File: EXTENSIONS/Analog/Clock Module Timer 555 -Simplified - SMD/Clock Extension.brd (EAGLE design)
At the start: 20 x 48 mm, 8 parts, among them X1 USB-A

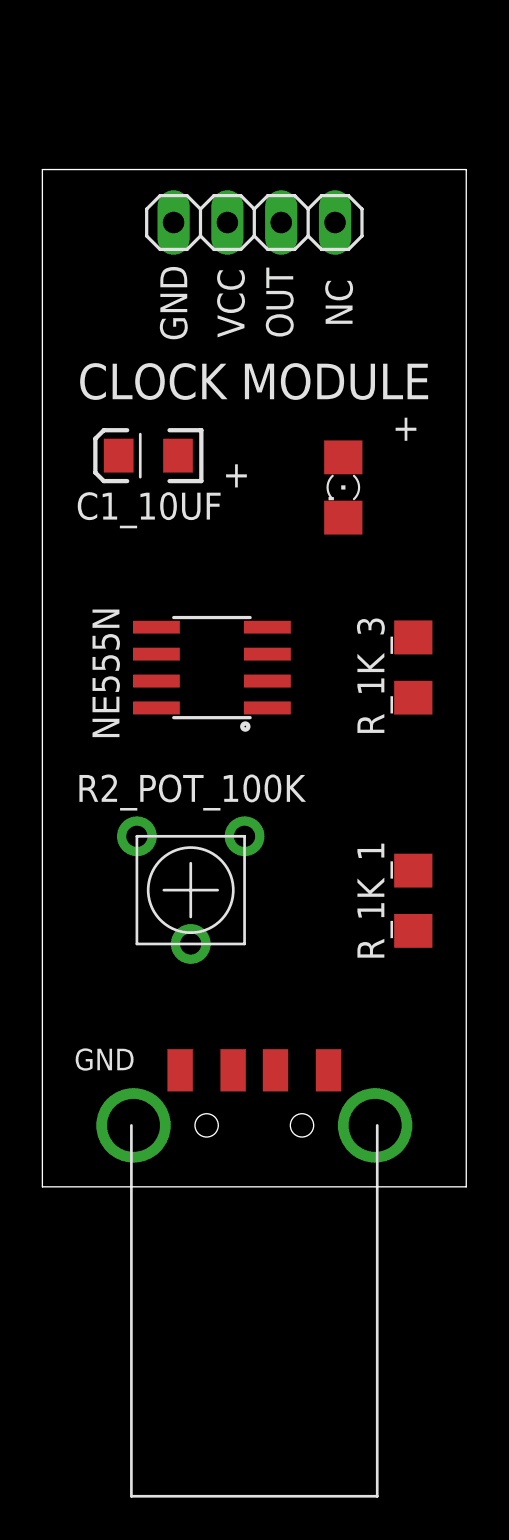
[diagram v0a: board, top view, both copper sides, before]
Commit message: Create new clock module SMD
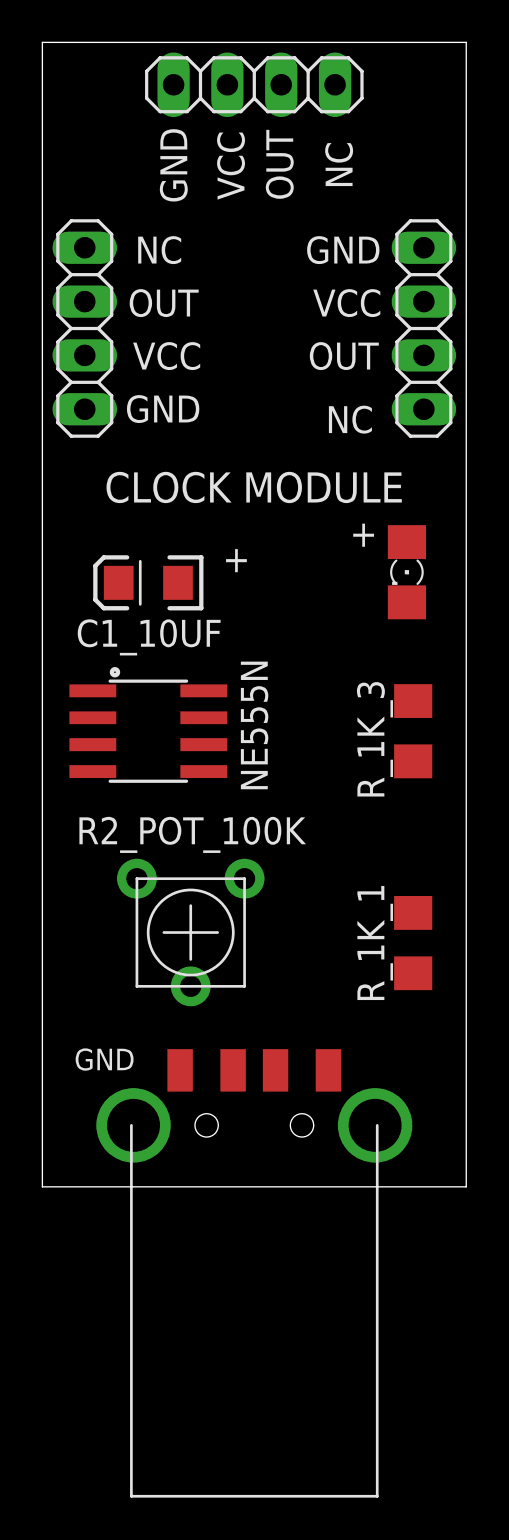
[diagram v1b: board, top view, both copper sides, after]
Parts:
- removed JP1: (no value), pinhead:1X04
- added OUT_1, OUT_2, OUT_3: (no value), pinhead:1X04
- moved C1_10UF 6.00 mm to (7.00, 40.5)
- moved LED_OUTPUT 5.00 mm to (19.2, 41.0)
- moved NE555N 4.24 mm to (7.00, 33.5), turned to 270 degrees
- moved R_1K_3 3.00 mm to (19.5, 33.5)
- moved R2_POT_100K 2.00 mm to (9.00, 24.0)
- moved R_1K_1 2.00 mm to (19.5, 23.5)
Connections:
- removed net TMR555_OUTPUT_REVERSE: JP1.4
- net GND: now also OUT_1.1, OUT_2.1, OUT_3.1; no longer JP1.1
- net TMR555_OUTPUT: now also OUT_1.3, OUT_2.3, OUT_3.3; no longer JP1.3
- net VCC: now also OUT_1.2, OUT_2.2, OUT_3.2; no longer JP1.2
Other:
- board size 20 x 48 mm -> 20 x 54 mm
- board text added: "PCBv1/SMD - 2019.12"
- board text removed: "PCBv3 - 2019.08"

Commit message: Fix bug in 4017-7Segment v2
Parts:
- moved LED_OUTPUT 13.0 mm to (12.2, 52.0)
- moved C1_10UF 5.10 mm to (12.0, 41.5)
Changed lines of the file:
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@@
 <text x="12" y="45" size="1.4224" layer="25" align="center">CLOCK MODULE</text>
 <text x="10.5" y="41" size="1.27" layer="25">+</text>
-<text x="16.5" y="42.2" size="1.27" layer="25">+</text>
+<text x="11.5" y="55.2" size="1.27" layer="25">+</text>
 <text x="16.2" y="56.2" size="1.27" layer="25" rot="R180" align="center">GND</text>
 <text x="16.4" y="53.7" size="1.27" layer="25" rot="R180" align="center">VCC</text>
@@
 <attribute name="VALUE" x="5.825" y="24" size="0.6096" layer="27" rot="R180"/>
 </element>
-<element name="LED_OUTPUT" library="adafruit" package="1206" value="" x="19.2" y="41" smashed="yes" rot="R270">
-<attribute name="VALUE" x="16.66" y="42.27" size="1.27" layer="27" rot="R270"/>
+<element name="LED_OUTPUT" library="adafruit" package="1206" value="" x="12.2" y="52" smashed="yes" rot="R270">
+<attribute name="VALUE" x="9.66" y="53.27" size="1.27" layer="27" rot="R270"/>
 </element>
 <element name="R_1K_3" library="adafruit" package="R1206" value="" x="19.5" y="33.5" smashed="yes" rot="R90">
@@
 <attribute name="VALUE" x="21.913" y="32.103" size="1.27" layer="27" rot="R90"/>
 </element>
-<element name="C1_10UF" library="SparkFun-Capacitors" package="EIA3216" value="10uF" x="7" y="40.5" smashed="yes" rot="R180">
-<attribute name="PROD_ID" value="CAP-00811" x="7" y="40.5" size="1.778" layer="27" rot="R180" display="off"/>
-<attribute name="NAME" x="7.04" y="38.119" size="1.27" layer="25" rot="R180" align="center"/>
-<attribute name="VALUE" x="6.592" y="39.168" size="0.4064" layer="27" rot="R180"/>
+<element name="C1_10UF" library="SparkFun-Capacitors" package="EIA3216" value="10uF" x="12" y="41.5" smashed="yes" rot="R180">
+<attribute name="PROD_ID" value="CAP-00811" x="12" y="41.5" size="1.778" layer="27" rot="R180" display="off"/>
+<attribute name="NAME" x="12.04" y="39.119" size="1.27" layer="25" rot="R180" align="center"/>
+<attribute name="VALUE" x="11.592" y="40.168" size="0.4064" layer="27" rot="R180"/>
 </element>
 <element name="NE555N" library="SparkFun-AnalogIC" package="SO08" value="" x="7" y="33.5" smashed="yes" rot="R270">
@@
 <contactref element="OUT_3" pad="1"/>
 <wire x1="8.19" y1="64" x2="20" y2="56.31" width="0" layer="19" extent="1-1"/>
-<wire x1="5.6" y1="40.5" x2="20" y2="56.31" width="0" layer="19" extent="1-1"/>
-<wire x1="4.3838" y1="35.405" x2="5.6" y2="40.5" width="0" layer="19" extent="1-1"/>
-<wire x1="19.5" y1="32.078" x2="4.3838" y2="35.405" width="0" layer="19" extent="1-1"/>
+<wire x1="4" y1="48.69" x2="8.19" y2="64" width="0" layer="19" extent="1-1"/>
+<wire x1="10.6" y1="41.5" x2="4" y2="48.69" width="0" layer="19" extent="1-1"/>
+<wire x1="4.3838" y1="35.405" x2="10.6" y2="41.5" width="0" layer="19" extent="1-1"/>
+<wire x1="19.5" y1="32.078" x2="10.6" y2="41.5" width="0" layer="19" extent="1-1"/>
 <wire x1="8.5" y1="17.5" x2="19.5" y2="32.078" width="0" layer="19" extent="1-1"/>
-<wire x1="4" y1="48.69" x2="8.5" y2="17.5" width="0" layer="19" extent="1-1"/>
 </signal>
 <signal name="VCC">
@@
 <contactref element="OUT_3" pad="2"/>
 <wire x1="20" y1="53.77" x2="10.73" y2="64" width="0" layer="19" extent="1-1"/>
-<wire x1="9.6162" y1="35.405" x2="20" y2="53.77" width="0" layer="19" extent="1-1"/>
+<wire x1="4" y1="51.23" x2="10.73" y2="64" width="0" layer="19" extent="1-1"/>
+<wire x1="9.6162" y1="35.405" x2="4" y2="51.23" width="0" layer="19" extent="1-1"/>
 <wire x1="4.3838" y1="31.595" x2="9.6162" y2="35.405" width="0" layer="19" extent="1-1"/>
 <wire x1="19.5" y1="24.922" x2="9.6162" y2="35.405" width="0" layer="19" extent="1-1"/>
 <wire x1="15.5" y1="17.5" x2="19.5" y2="24.922" width="0" layer="19" extent="1-1"/>
-<wire x1="4" y1="51.23" x2="15.5" y2="17.5" width="0" layer="19" extent="1-1"/>
 </signal>
 <signal name="DIS">
@@
 <contactref element="NE555N" pad="2"/>
 <contactref element="NE555N" pad="6"/>
-<wire x1="4.3838" y1="34.135" x2="8.4" y2="40.5" width="0" layer="19" extent="1-1"/>
-<wire x1="9.6162" y1="32.865" x2="4.3838" y2="34.135" width="0" layer="19" extent="1-1"/>
+<wire x1="9.6162" y1="32.865" x2="13.4" y2="41.5" width="0" layer="19" extent="1-1"/>
+<wire x1="4.3838" y1="34.135" x2="9.6162" y2="32.865" width="0" layer="19" extent="1-1"/>
 <wire x1="9" y1="21.46" x2="9.6162" y2="32.865" width="0" layer="19" extent="1-1"/>
 </signal>
@@
 <contactref element="OUT_2" pad="3"/>
 <contactref element="OUT_3" pad="3"/>
-<wire x1="20" y1="51.23" x2="13.27" y2="64" width="0" layer="19" extent="1-1"/>
-<wire x1="19.2" y1="42.422" x2="20" y2="51.23" width="0" layer="19" extent="1-1"/>
-<wire x1="4.3838" y1="32.865" x2="19.2" y2="42.422" width="0" layer="19" extent="1-1"/>
-<wire x1="4" y1="53.77" x2="4.3838" y2="32.865" width="0" layer="19" extent="1-1"/>
+<wire x1="12.2" y1="53.422" x2="13.27" y2="64" width="0" layer="19" extent="1-1"/>
+<wire x1="20" y1="51.23" x2="12.2" y2="53.422" width="0" layer="19" extent="1-1"/>
+<wire x1="4" y1="53.77" x2="12.2" y2="53.422" width="0" layer="19" extent="1-1"/>
+<wire x1="4.3838" y1="32.865" x2="4" y2="53.77" width="0" layer="19" extent="1-1"/>
 </signal>
 <signal name="N$5">
 <contactref element="LED_OUTPUT" pad="C"/>
 <contactref element="R_1K_3" pad="2"/>
-<wire x1="19.5" y1="34.922" x2="19.2" y2="39.578" width="0" layer="19" extent="1-1"/>
+<wire x1="19.5" y1="34.922" x2="12.2" y2="50.578" width="0" layer="19" extent="1-1"/>
 </signal>
 </signals>

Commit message: Create v3 of 0 to 99 counter
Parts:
- renumbered R_1K_3 to R_1K_2
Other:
- board text added: "PCB v1 /smd - 2019.12"
- board text removed: "PCBv1/SMD - 2019.12"
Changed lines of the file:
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@@
 <layer number="23" name="tOrigins" color="15" fill="1" visible="yes" active="yes"/>
 <layer number="24" name="bOrigins" color="15" fill="1" visible="yes" active="yes"/>
-<layer number="25" name="tNames" color="7" fill="1" visible="yes" active="yes"/>
-<layer number="26" name="bNames" color="7" fill="1" visible="no" active="yes"/>
+<layer number="25" name="tNames" color="7" fill="1" visible="no" active="yes"/>
+<layer number="26" name="bNames" color="7" fill="1" visible="yes" active="yes"/>
 <layer number="27" name="tValues" color="7" fill="1" visible="no" active="yes"/>
 <layer number="28" name="bValues" color="7" fill="1" visible="no" active="yes"/>
@@
 <wire x1="22" y1="66" x2="2" y2="66" width="0" layer="20"/>
 <wire x1="2" y1="66" x2="2" y2="12" width="0" layer="20"/>
-<text x="19" y="35.7" size="2.1844" layer="26" rot="SMR270" align="center">MadeInTheUSB.net</text>
-<text x="12" y="53.5" size="1.016" layer="26" rot="MR0" align="center">PCBv1/SMD - 2019.12</text>
+<text x="12" y="42.7" size="2.1844" layer="26" rot="SMR270" align="center">MadeInTheUSB.net</text>
+<text x="12" y="59.5" size="1.016" layer="26" rot="MR0" align="center">PCB v1 /smd - 2019.12</text>
 <text x="8.2" y="60.2" size="1.27" layer="25" rot="R90" align="center">GND</text>
 <text x="13.2" y="60.2" size="1.27" layer="25" rot="R90" align="center">OUT</text>
@@
 <attribute name="VALUE" x="9.66" y="53.27" size="1.27" layer="27" rot="R270"/>
 </element>
-<element name="R_1K_3" library="adafruit" package="R1206" value="" x="19.5" y="33.5" smashed="yes" rot="R90">
+<element name="R_1K_2" library="adafruit" package="R1206" value="" x="19.5" y="33.5" smashed="yes" rot="R90">
 <attribute name="NAME" x="17.5" y="33.103" size="1.27" layer="25" rot="R90" align="center"/>
 <attribute name="VALUE" x="21.913" y="32.103" size="1.27" layer="27" rot="R90"/>
@@
 <contactref element="X1" pad="4"/>
 <contactref element="OUT_1" pad="1"/>
-<contactref element="R_1K_3" pad="1"/>
+<contactref element="R_1K_2" pad="1"/>
 <contactref element="C1_10UF" pad="A"/>
 <contactref element="NE555N" pad="1"/>
@@
 <signal name="N$5">
 <contactref element="LED_OUTPUT" pad="C"/>
-<contactref element="R_1K_3" pad="2"/>
+<contactref element="R_1K_2" pad="2"/>
 <wire x1="19.5" y1="34.922" x2="12.2" y2="50.578" width="0" layer="19" extent="1-1"/>
 </signal>

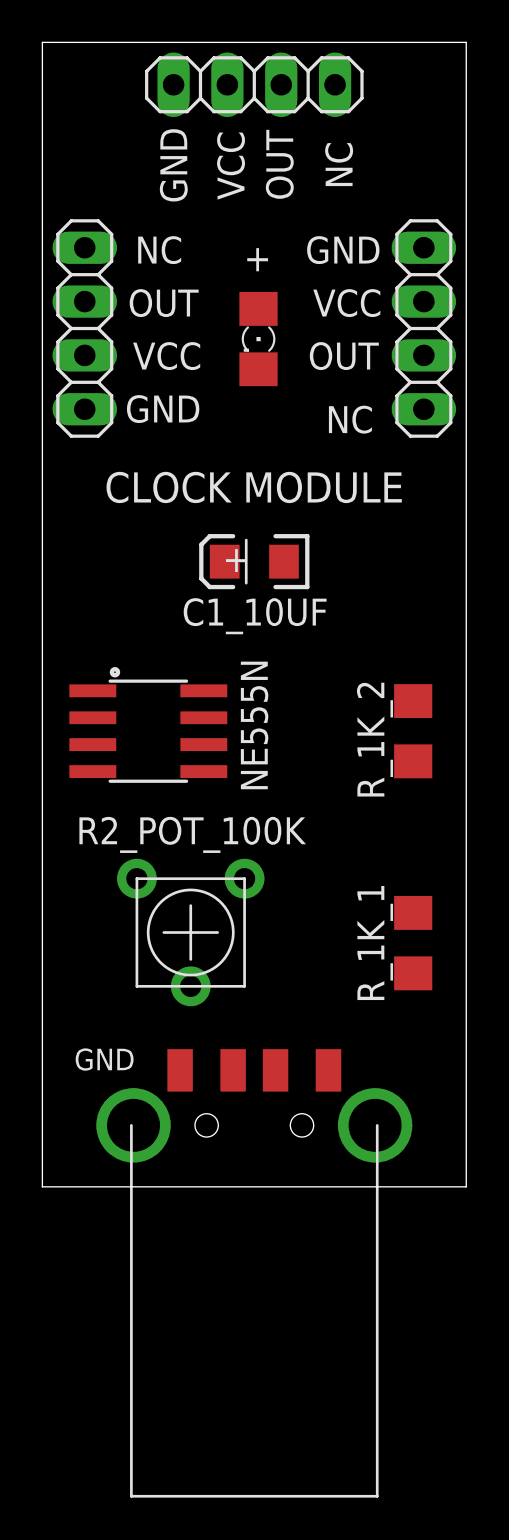
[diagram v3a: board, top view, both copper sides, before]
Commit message: Create v3 of 0 to 99 counter
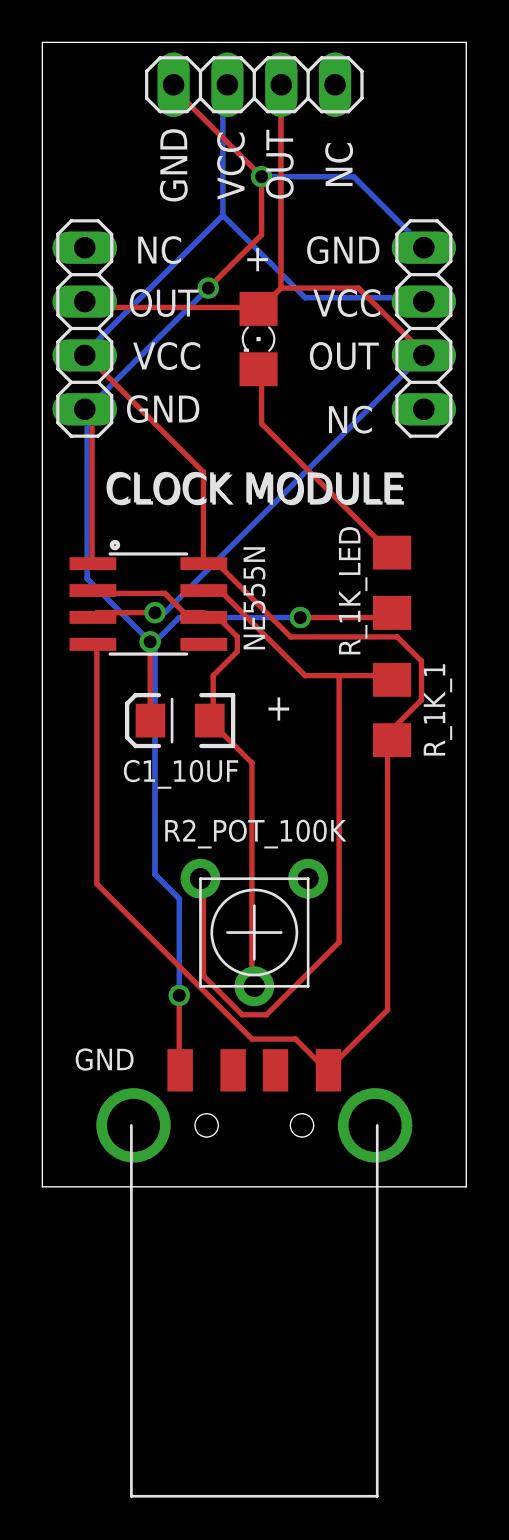
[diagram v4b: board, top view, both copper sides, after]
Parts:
- removed R_1K_2: (no value), adafruit:R1206
- added R_1K_LED: (no value), adafruit:R1206
- moved R_1K_1 11.0 mm to (18.5, 34.5), turned to 270 degrees
- moved C1_10UF 8.28 mm to (8.50, 34.0)
- moved NE555N 6.00 mm to (7.00, 39.5)
- moved R2_POT_100K 3.00 mm to (12.0, 24.0)
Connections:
- net GND: now also R_1K_LED.1; no longer R_1K_2.1
- net N$5: now also R_1K_LED.2; no longer R_1K_2.2
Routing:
- net VCC: track 0.00 -> 98.2 mm
- net GND: track 0.00 -> 85.6 mm, vias 0 -> 5
- net TMR555_OUTPUT: track 0.00 -> 48.2 mm, vias 0 -> 1
- net DIS: track 0.00 -> 36.5 mm
- net THRESHOLD: track 0.00 -> 25.8 mm
- net N$5: track 0.00 -> 11.3 mm
